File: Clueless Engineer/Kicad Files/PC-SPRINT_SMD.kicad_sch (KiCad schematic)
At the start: 16 parts, among them J1 TB1, U1 8284A, U2 8284A, U3 8284A, X1 22.11 MHz

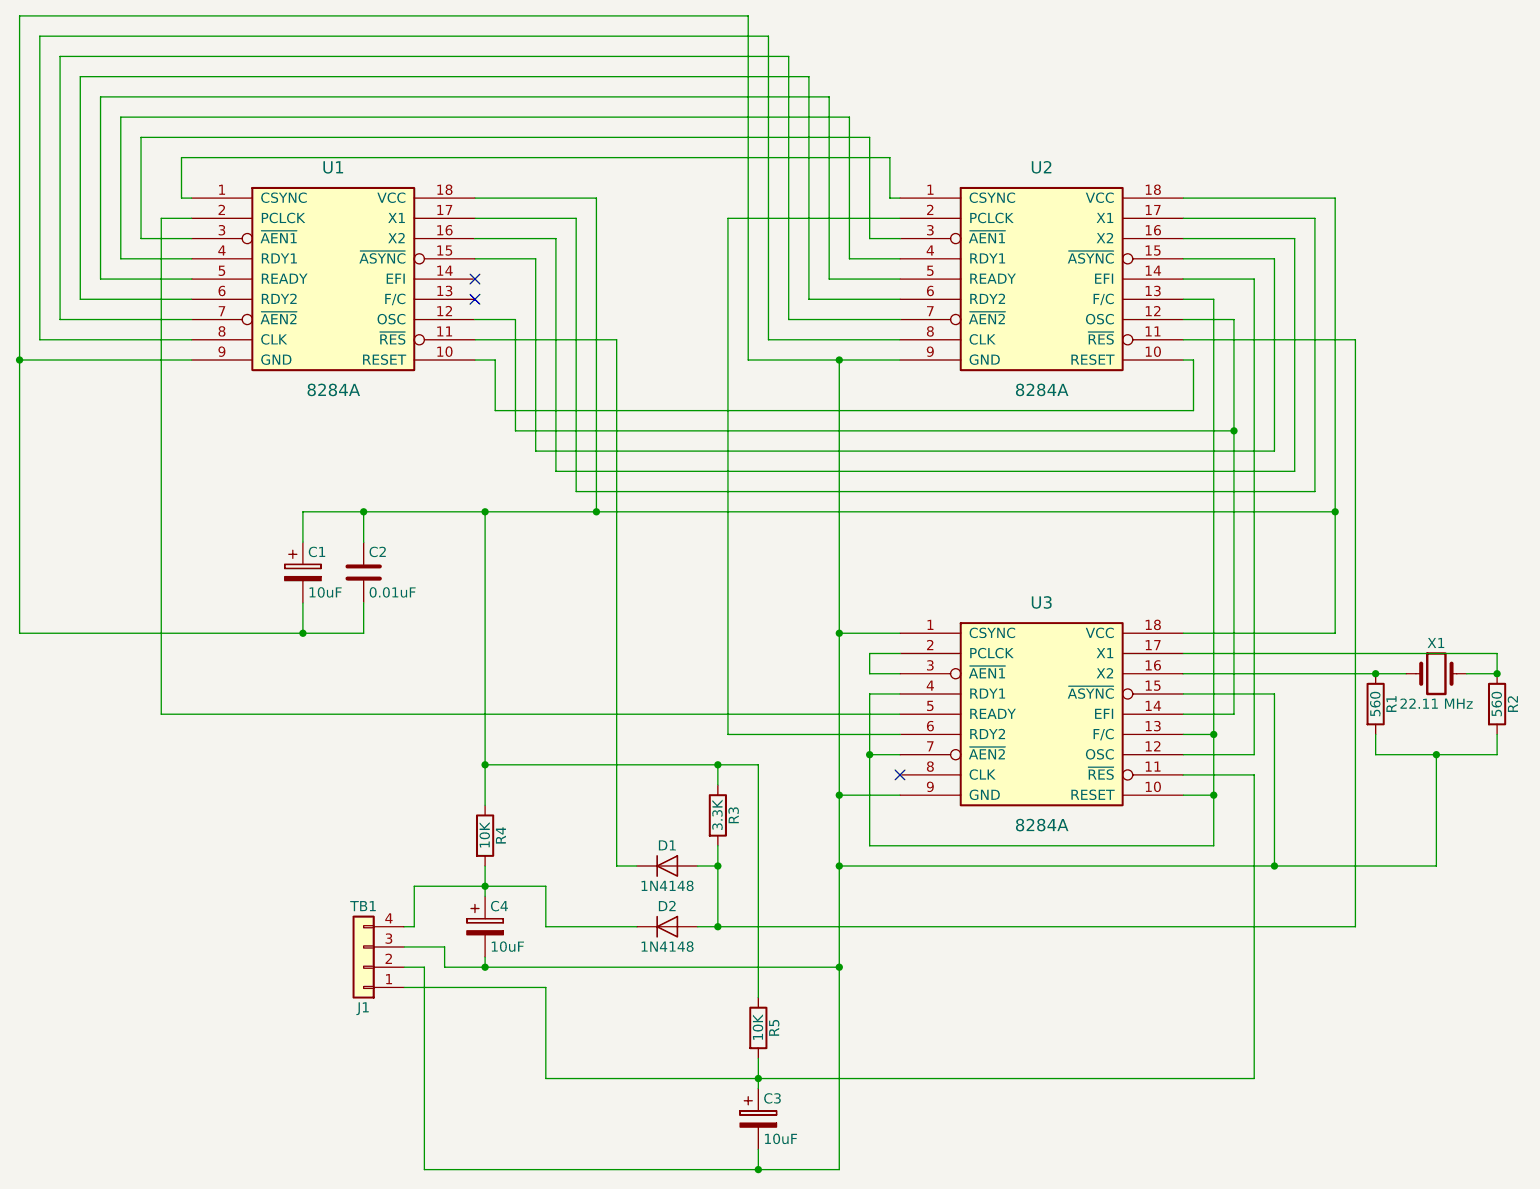
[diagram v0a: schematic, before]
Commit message: Shrunk PCB to 24mm (from original 29.1mm)
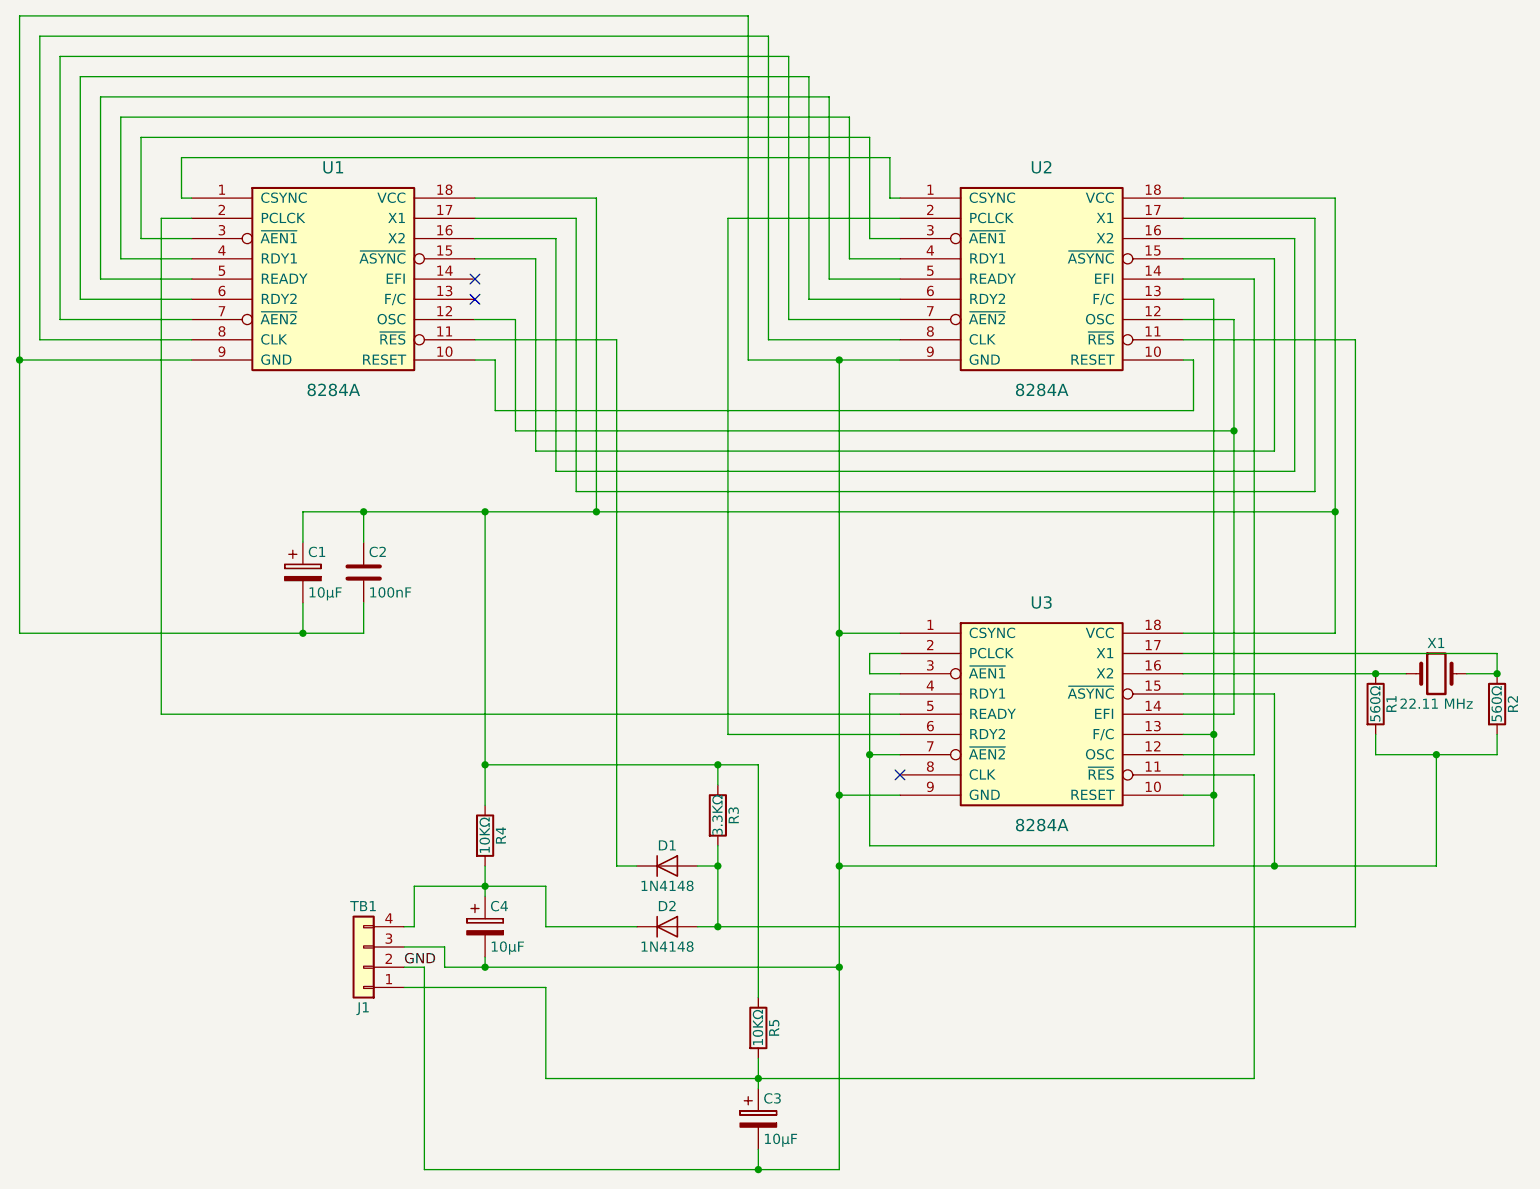
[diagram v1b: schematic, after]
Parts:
- C1, C3, C4: value 10uF -> 10µF
- C2: value 0.01uF -> 100nF
- R1, R2: value 560 -> 560Ω
- R3: value 3.3K -> 3.3KΩ
- R4, R5: value 10K -> 10KΩ
- U1: footprint Package_DIP:DIP-18_W7.62mm_LongPads -> Package_DIP:DIP-18_W7.62mm_Socket
- U2, U3: footprint Package_DIP:DIP-18_W7.62mm_LongPads -> Package_DIP:DIP-18_W7.62mm
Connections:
- net GND: now reaches C1.2, C2.2, C3.2, C4.2, J1.2 (Pin_2), J1.3 (Pin_3), R1.2, R2.2, U1.9 (GND), U2.9 (GND), U3.1 (CSYNC), U3.15 (~{ASYNC}), U3.9 (GND)
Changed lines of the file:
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@@
     (stroke (width 0) (type default))
   )
+  (label "GND" (at 88.9 143.51 0) (fields_autoplaced)
+    (effects (font (size 1.27 1.27)) (justify left bottom))
+  )
   (symbol (lib_id "PC-SPRINT-rescue:8284A") (at 80.01 57.15 0) (unit 1)
     (in_bom yes) (on_board yes) (dnp no)
@@
       (effects (font (size 1.524 1.524)))
     )
-    (property "Footprint" "Package_DIP:DIP-18_W7.62mm_LongPads" (at 78.74 57.15 0)
+    (property "Footprint" "Package_DIP:DIP-18_W7.62mm_Socket" (at 78.74 57.15 0)
       (effects (font (size 1.524 1.524)) hide)
     )
@@
       (effects (font (size 1.524 1.524)))
     )
-    (property "Footprint" "Package_DIP:DIP-18_W7.62mm_LongPads" (at 167.64 57.15 0)
+    (property "Footprint" "Package_DIP:DIP-18_W7.62mm" (at 167.64 57.15 0)
       (effects (font (size 1.524 1.524)) hide)
     )
@@
       (effects (font (size 1.524 1.524)))
     )
-    (property "Footprint" "Package_DIP:DIP-18_W7.62mm_LongPads" (at 167.64 111.76 0)
+    (property "Footprint" "Package_DIP:DIP-18_W7.62mm" (at 167.64 111.76 0)
       (effects (font (size 1.524 1.524)) hide)
     )
@@
       (effects (font (size 1.27 1.27)) (justify left))
     )
-    (property "Value" "10uF" (at 76.835 96.52 0)
+    (property "Value" "10µF" (at 76.835 96.52 0)
       (effects (font (size 1.27 1.27)) (justify left))
     )
@@
       (effects (font (size 1.27 1.27)) (justify left))
     )
-    (property "Value" "10uF" (at 133.985 165.1 0)
+    (property "Value" "10µF" (at 133.985 165.1 0)
       (effects (font (size 1.27 1.27)) (justify left))
     )
@@
       (effects (font (size 1.27 1.27)) (justify left))
     )
-    (property "Value" "10uF" (at 99.695 140.97 0)
+    (property "Value" "10µF" (at 99.695 140.97 0)
       (effects (font (size 1.27 1.27)) (justify left))
     )
@@
       (effects (font (size 1.27 1.27)) (justify left))
     )
-    (property "Value" "0.01uF" (at 84.455 96.52 0)
+    (property "Value" "100nF" (at 84.455 96.52 0)
       (effects (font (size 1.27 1.27)) (justify left))
     )
@@
       (effects (font (size 1.27 1.27)))
     )
-    (property "Value" "560" (at 210.82 110.49 90)
+    (property "Value" "560Ω" (at 210.82 110.49 90)
       (effects (font (size 1.27 1.27)))
     )
@@
       (effects (font (size 1.27 1.27)))
     )
-    (property "Value" "560" (at 226.06 110.49 90)
+    (property "Value" "560Ω" (at 226.06 110.49 90)
       (effects (font (size 1.27 1.27)))
     )
@@
       (effects (font (size 1.27 1.27)))
     )
-    (property "Value" "3.3K" (at 128.27 124.46 90)
+    (property "Value" "3.3KΩ" (at 128.27 124.46 90)
       (effects (font (size 1.27 1.27)))
     )
@@
       (effects (font (size 1.27 1.27)))
     )
-    (property "Value" "10K" (at 99.06 127 90)
+    (property "Value" "10KΩ" (at 99.06 127 90)
       (effects (font (size 1.27 1.27)))
     )
@@
       (effects (font (size 1.27 1.27)))
     )
-    (property "Value" "10K" (at 133.35 151.13 90)
-      (effects (font (size 1.27 1.27)))
-    )
+    (property "Value" "10KΩ" (at 133.35 151.13 90)
+      (effects (font (size 1.27 1.27)))
+    )
